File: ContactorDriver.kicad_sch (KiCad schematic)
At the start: 42 parts, among them J1 PowerConn, J10 FanConn3, J11 FanConn4, J2 DashboardConnA, J3 ContactorAConn, J4 DashboardConnB, J5 ContactorBConn, J6 DashboardConnC, J7 ContactorCConn, J8 FanConn1, J9 FanConn2, Q1 NDS356AP-VB, Q2 IRLML0030TRPbF, Q3 IRLML0030TRPbF, Q4 IRLML0030TRPbF

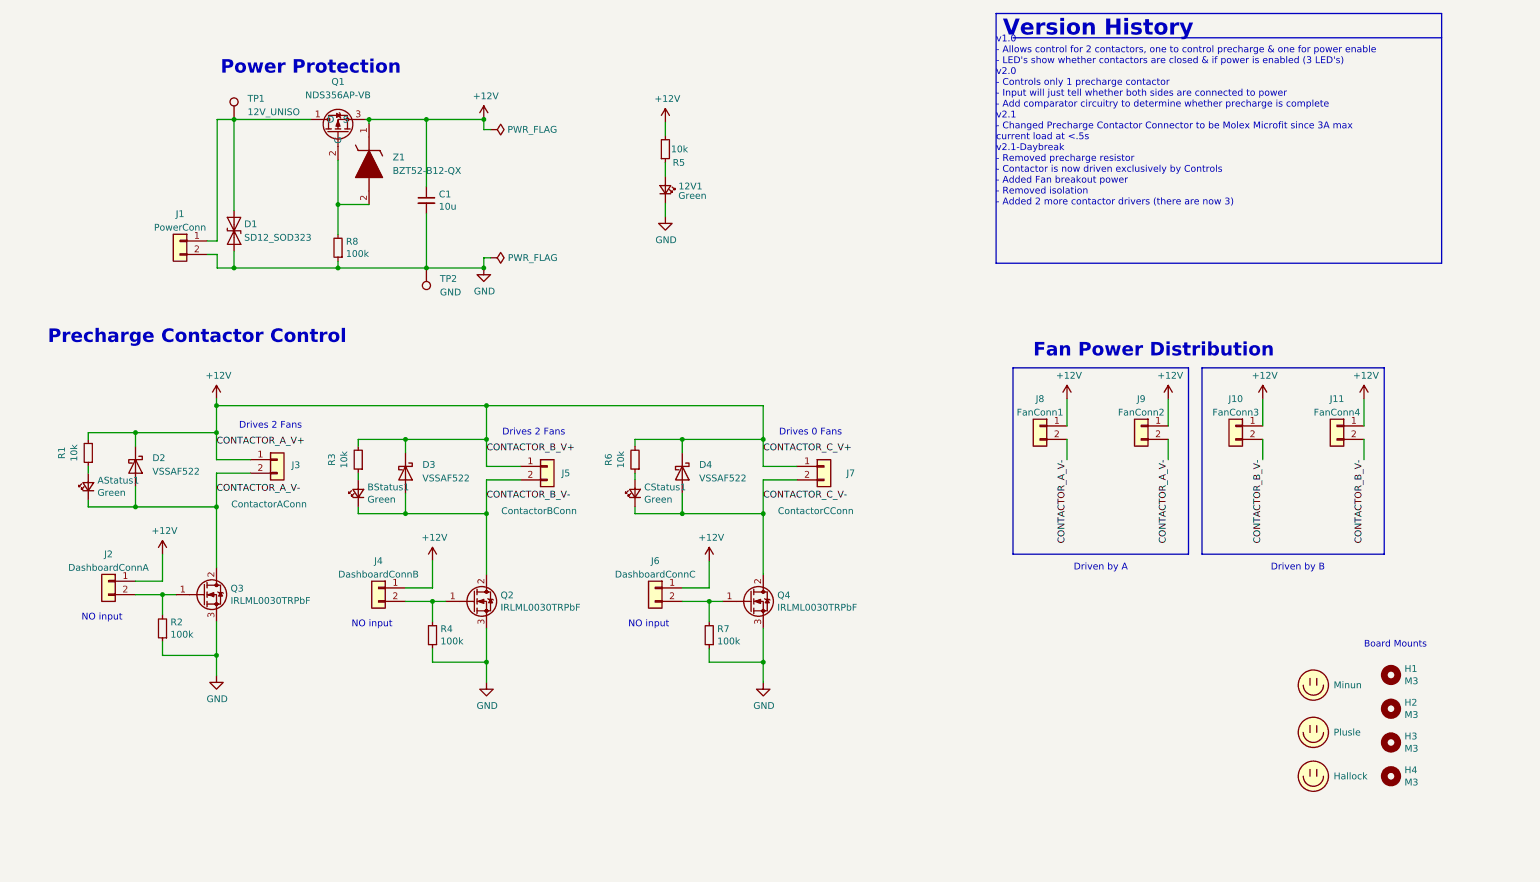
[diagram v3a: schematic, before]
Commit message: Updated BOM, PDFs, and added labels for tps
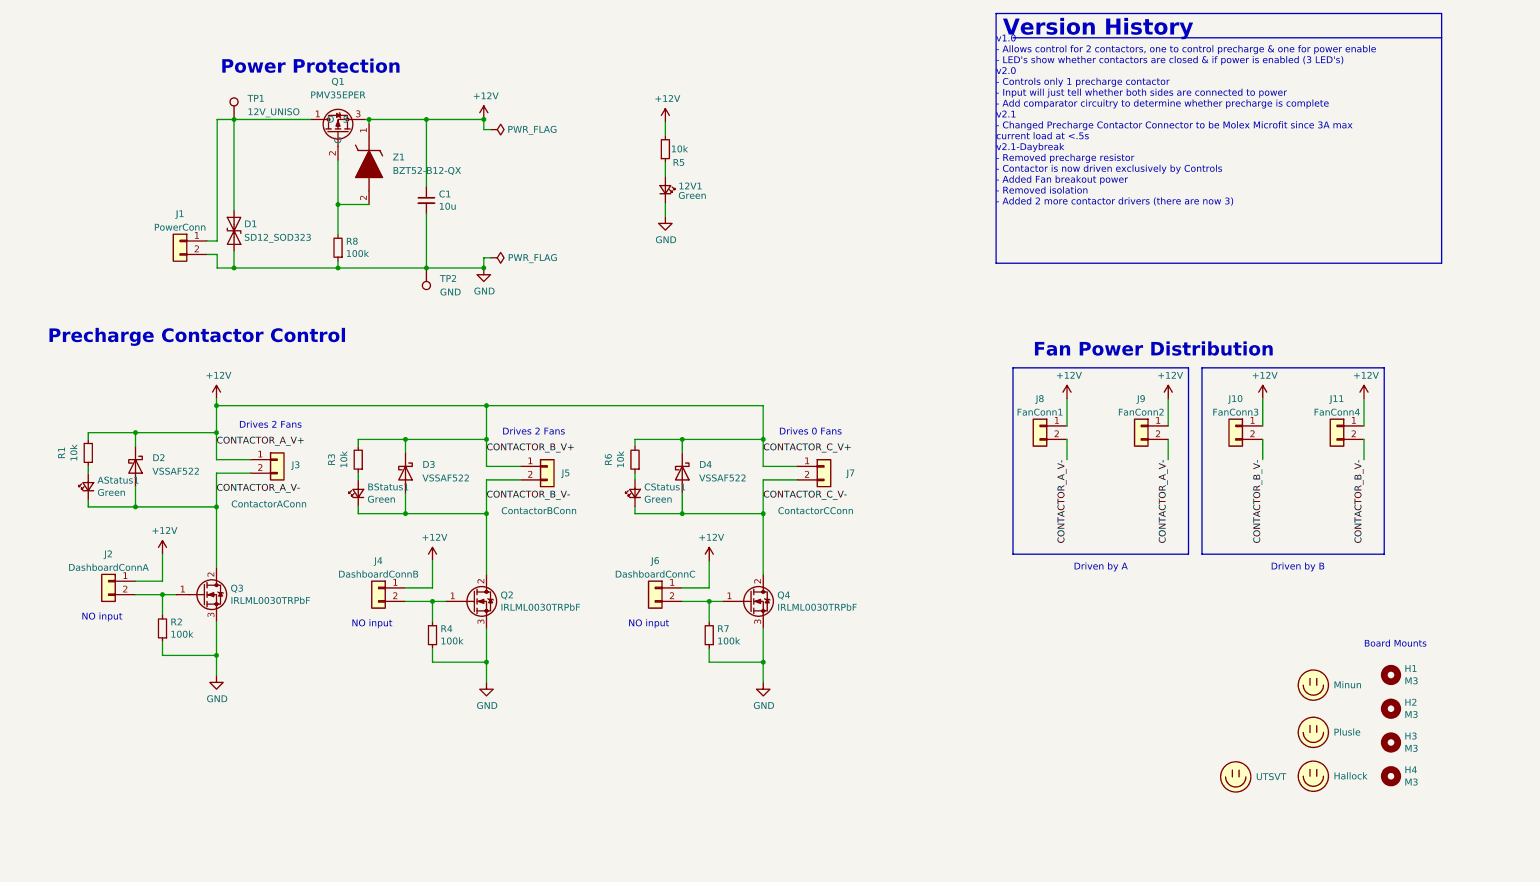
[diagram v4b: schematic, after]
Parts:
- added LOGO4: UTSVT, UTSVT_Special:UTSVT_Logo_Symbol, symbol utsvt-misc:Logo_Placeholder
- Q1: value NDS356AP-VB -> PMV35EPER; footprint Package_TO_SOT_SMD:SOT-23 -> Package_TO_SOT_SMD:SOT-23-3
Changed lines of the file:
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@@
 			)
 		)
-		(property "Value" "NDS356AP-VB"
+		(property "Value" "PMV35EPER"
 			(at 74.93 29.21 90)
 			(effects
@@
 			)
 		)
-		(property "Footprint" "Package_TO_SOT_SMD:SOT-23"
+		(property "Footprint" "Package_TO_SOT_SMD:SOT-23-3"
 			(at 61.722 34.798 0)
 			(effects
@@
 			)
 		)
-		(property "Datasheet" "https://www.lcsc.com/datasheet/lcsc_datasheet_2211010930_VBsemi-Elec-NDS356AP-VB_C710027.pdf"
+		(property "Datasheet" "https://www.mouser.com/datasheet/2/916/PMV35EPE-1539905.pdf"
 			(at 88.138 29.718 0)
 			(effects
@@
 			)
 		)
-		(property "Description" "30V 5.6A 46mΩ@10V,4.4A 2.5W 2V@250uA 1 Piece P-Channel SOT-23 MOSFETs ROHS"
+		(property "Description" "30V 5.3A 45mΩ@10V,4.4A 2.5W 2V@250uA 1 Piece P-Channel SOT-23 MOSFETs ROHS"
 			(at 90.932 27.686 0)
 			(effects
@@
 					(unit 1)
 				)
+			)
+		)
+	)
+	(symbol
+		(lib_id "utsvt-misc:Logo_Placeholder")
+		(at 243.84 157.48 0)
+		(unit 1)
+		(exclude_from_sim no)
+		(in_bom yes)
+		(on_board yes)
+		(dnp no)
+		(fields_autoplaced yes)
+		(property "Reference" "LOGO4"
+			(at 243.84 153.67 0)
+			(effects
+				(font
+					(size 1.27 1.27)
+				)
+				(hide yes)
+			)
+		)
+		(property "Value" "UTSVT"
+			(at 247.65 157.4799 0)
+			(effects
+				(font
+					(size 1.27 1.27)
+				)
+				(justify left)
+			)
+		)
+		(property "Footprint" "UTSVT_Special:UTSVT_Logo_Symbol"
+			(at 243.84 155.575 0)
+			(effects
+				(font
+					(size 1.27 1.27)
+				)
+				(hide yes)
+			)
+		)
+		(property "Datasheet" ""
+			(at 243.84 155.575 0)
+			(effects
+				(font
+					(size 1.27 1.27)
+				)
+				(hide yes)
+			)
+		)
+		(property "Description" "Graph footprint placeholder"
+			(at 243.84 157.48 0)
+			(effects
+				(font
+					(size 1.27 1.27)
+				)
+				(hide yes)
+			)
+		)
+		(instances
+			(project "ContactorDriver"
+				(path "/aaa5c8ef-bb12-4c4a-bd2b-ddbca3d09ae8"
+					(reference "LOGO4")
+					(unit 1)
+				)

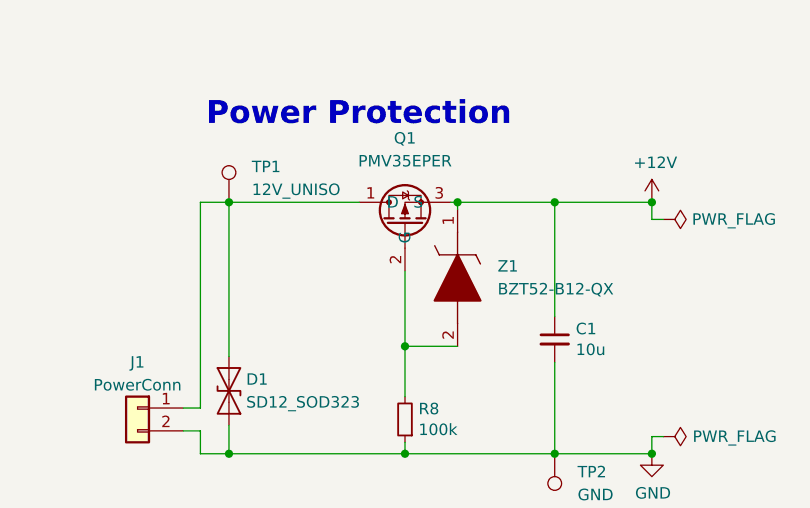
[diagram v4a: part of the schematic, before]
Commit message: fixed the pmos pinout
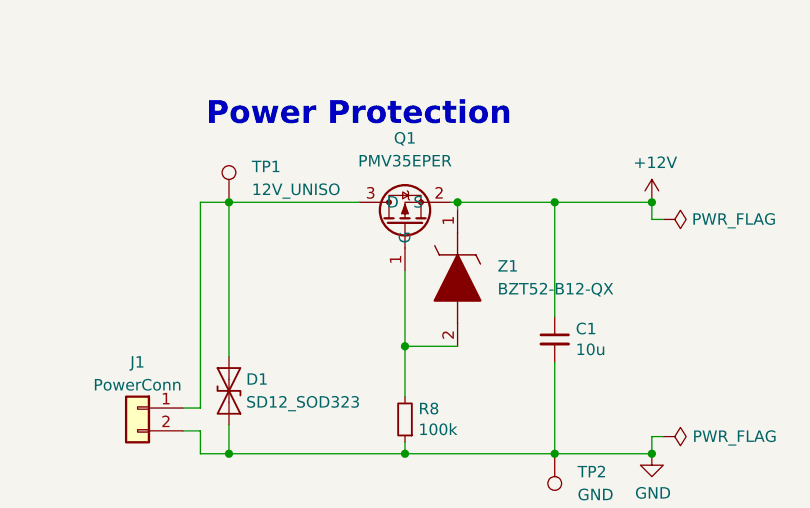
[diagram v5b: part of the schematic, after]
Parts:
- Q1: footprint Package_TO_SOT_SMD:SOT-23-3 -> Package_TO_SOT_SMD:SOT-23; symbol utsvt-chips:NDS356AP-VB -> utsvt-chips:PMV35EPE
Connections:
- net +12V: now also Q1.2 (S); no longer Q1.3 (S)
- net at D1.2 (A2), J1.1 (Pin_1), TP1.1: now also Q1.3 (D); no longer Q1.1 (D)
- net at R8.2, Z1.2: now also Q1.1 (G); no longer Q1.2 (G)
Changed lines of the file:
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@@
 	)
 	(symbol
-		(lib_id "utsvt-chips:NDS356AP-VB")
+		(lib_id "utsvt-chips:PMV35EPE")
 		(at 74.93 35.052 90)
 		(unit 1)
@@
 			)
 		)
-		(property "Footprint" "Package_TO_SOT_SMD:SOT-23-3"
+		(property "Footprint" "Package_TO_SOT_SMD:SOT-23"
 			(at 61.722 34.798 0)
 			(effects
@@
 			)
 		)
-		(property "Description" "30V 5.3A 45mΩ@10V,4.4A 2.5W 2V@250uA 1 Piece P-Channel SOT-23 MOSFETs ROHS"
+		(property "Description" "30 V, P-channel Trench MOSFET"
 			(at 90.932 27.686 0)
 			(effects

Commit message: added sense
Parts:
- removed J2: DashboardConnA, Connector_Molex:Molex_Micro-Fit_3.0_43650-0215_1x02_P3.00mm_Vertical, symbol Connector_Generic:Conn_01x02
- removed J3: ContactorAConn, Connector_Molex:Molex_Micro-Fit_3.0_43650-0215_1x02_P3.00mm_Vertical, symbol Connector_Generic:Conn_01x02
- removed J4: DashboardConnB, Connector_Molex:Molex_Micro-Fit_3.0_43650-0215_1x02_P3.00mm_Vertical, symbol Connector_Generic:Conn_01x02
- removed J5: ContactorBConn, Connector_Molex:Molex_Micro-Fit_3.0_43650-0215_1x02_P3.00mm_Vertical, symbol Connector_Generic:Conn_01x02
- removed J6: DashboardConnC, Connector_Molex:Molex_Micro-Fit_3.0_43650-0215_1x02_P3.00mm_Vertical, symbol Connector_Generic:Conn_01x02
- removed J7: ContactorCConn, Connector_Molex:Molex_Micro-Fit_3.0_43650-0215_1x02_P3.00mm_Vertical, symbol Connector_Generic:Conn_01x02
- added J12: ContactorAConn, UTSVT_Connectors:Molex_MicroFit3.0_1x4xP3.00mm_PolarizingPeg_Vertical, symbol Connector_Generic:Conn_01x04
- added J2: DashboardConnA, UTSVT_Connectors:Molex_MicroFit3.0_1x4xP3.00mm_PolarizingPeg_Vertical, symbol Connector_Generic:Conn_01x04
- added J3: ContactorBConn, UTSVT_Connectors:Molex_MicroFit3.0_1x4xP3.00mm_PolarizingPeg_Vertical, symbol Connector_Generic:Conn_01x04
- added J4: DashboardConnB, UTSVT_Connectors:Molex_MicroFit3.0_1x4xP3.00mm_PolarizingPeg_Vertical, symbol Connector_Generic:Conn_01x04
- added J5: ContactorCConn, UTSVT_Connectors:Molex_MicroFit3.0_1x4xP3.00mm_PolarizingPeg_Vertical, symbol Connector_Generic:Conn_01x04
- added J6: DashboardConnC, UTSVT_Connectors:Molex_MicroFit3.0_1x4xP3.00mm_PolarizingPeg_Vertical, symbol Connector_Generic:Conn_01x04
- added R10, R11, R9: 510, Resistor_SMD:R_0805_2012Metric_Pad1.20x1.40mm_HandSolder, symbol Device:R
- added U1, U2, U3: SFH617A-1, Package_DIP:DIP-4_W7.62mm, symbol Isolator:SFH617A-1
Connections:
- net +12V: now also J12.1 (Pin_1), J12.3 (Pin_3), J2.4 (Pin_4), J3.1 (Pin_1), J3.3 (Pin_3), J4.4 (Pin_4), J5.1 (Pin_1), J5.3 (Pin_3), J6.4 (Pin_4)
- net CONTACTOR_A_V-: now also J12.2 (Pin_2)
- net CONTACTOR_B_V-: now also J3.2 (Pin_2)
- net CONTACTOR_C_V-: now also J5.2 (Pin_2)
- net at Q3.1 (G), R2.2: now also J2.3 (Pin_3)
- net at Q4.1 (G), R7.2: now also J6.3 (Pin_3)
- net at Q2.1 (G), R4.2: now also J4.3 (Pin_3)
- new net: R10.2, U2.1
- new net: R9.2, U1.1
- new net: R11.2, U3.1
- new net AUX_A+: J2.2 (Pin_2), U1.4
- new net AUX_A-: J2.1 (Pin_1), U1.3
- new net AUX_B+: J4.2 (Pin_2), U2.4
- new net AUX_B-: J4.1 (Pin_1), U2.3
- new net AUX_C+: J6.2 (Pin_2), U3.4
- new net AUX_C-: J6.1 (Pin_1), U3.3
- new net GNDPWR: U1.2, U2.2, U3.2
- new net SENSE_A: J12.4 (Pin_4), R9.1
- new net SENSE_B: J3.4 (Pin_4), R10.1
- new net SENSE_C: J5.4 (Pin_4), R11.1
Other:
- note removed: "NO input"
- moved on the sheet: AStatus1, BStatus1, CStatus1, D2, D3, D4, J10, J11, J8, J9, Q2, Q3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

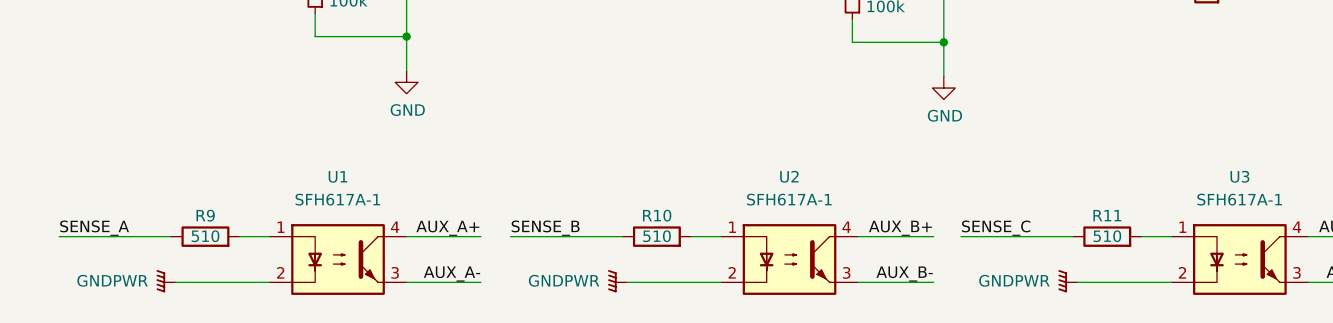
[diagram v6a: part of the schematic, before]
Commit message: layout changes for sense
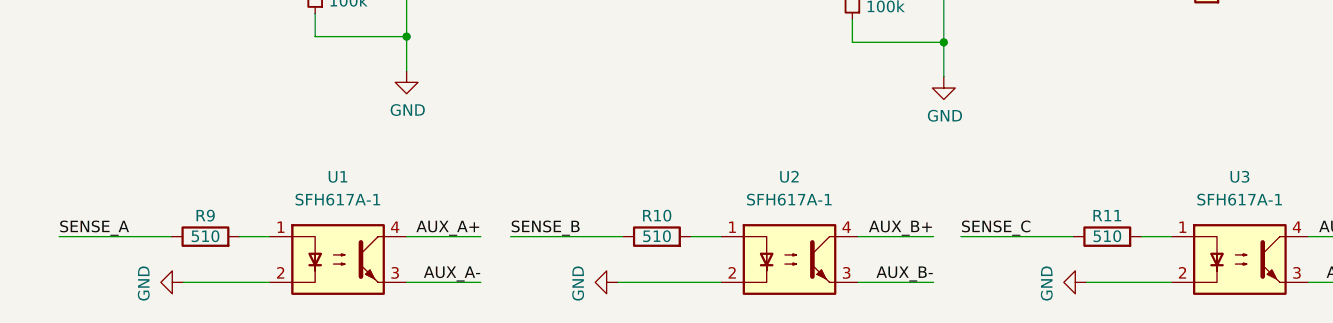
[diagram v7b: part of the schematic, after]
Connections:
- net GNDPWR is gone; now on net GND: U1.2, U2.2, U3.2
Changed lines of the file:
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@@
 	(wire
 		(pts
-			(xy 30.861 161.29) (xy 41.275 161.29)
+			(xy 132.08 161.29) (xy 141.478 161.29)
 		)
 		(stroke
@@
 	(wire
 		(pts
+			(xy 80.01 161.29) (xy 91.44 161.29)
+		)
+		(stroke
+			(width 0)
+			(type default)
+		)
+	)
+	(wire
+		(pts
 			(xy 55.372 33.782) (xy 55.372 50.927)
 		)
@@
 	(wire
 		(pts
-			(xy 131.064 161.29) (xy 141.478 161.29)
-		)
-		(stroke
-			(width 0)
-			(type default)
-		)
-	)
-	(wire
-		(pts
 			(xy 176.53 93.345) (xy 176.53 98.425)
 		)
@@
 	(wire
 		(pts
+			(xy 31.75 161.29) (xy 41.275 161.29)
+		)
+		(stroke
+			(width 0)
+			(type default)
+		)
+	)
+	(wire
+		(pts
 			(xy 55.372 58.547) (xy 55.372 61.722)
 		)
@@
 	(wire
 		(pts
-			(xy 81.026 161.29) (xy 91.44 161.29)
-		)
-		(stroke
-			(width 0)
-			(type default)
-		)
-	)
-	(wire
-		(pts
 			(xy 176.53 98.425) (xy 194.31 98.425)
 		)
@@
 	)
 	(symbol
+		(lib_id "power:GND")
+		(at 132.08 161.29 270)
+		(unit 1)
+		(exclude_from_sim no)
+		(in_bom yes)
+		(on_board yes)
+		(dnp no)
+		(property "Reference" "#PWR021"
+			(at 125.73 161.29 0)
+			(effects
+				(font
+					(size 1.27 1.27)
+				)
+				(hide yes)
+			)
+		)
+		(property "Value" "GND"
+			(at 127.6858 161.417 0)
+			(effects
+				(font
+					(size 1.27 1.27)
+				)
+			)
+		)
+		(property "Footprint" ""
+			(at 132.08 161.29 0)
+			(effects
+				(font
+					(size 1.27 1.27)
+				)
+				(hide yes)
+			)
+		)
+		(property "Datasheet" ""
+			(at 132.08 161.29 0)
+			(effects
+				(font
+					(size 1.27 1.27)
+				)
+				(hide yes)
+			)
+		)
+		(property "Description" ""
+			(at 132.08 161.29 0)
+			(effects
+				(font
+					(size 1.27 1.27)
+				)
+				(hide yes)
+			)
+		)
+		(pin "1"
+		)
+		(instances
+			(project "ContactorDriver"
+				(path "/aaa5c8ef-bb12-4c4a-bd2b-ddbca3d09ae8"
+					(reference "#PWR021")
+					(unit 1)
+				)
+			)
+		)
+	)
+	(symbol
 		(lib_id "Connector_Generic:Conn_01x02")
 		(at 234.315 81.915 0)
@@
 	)
 	(symbol
-		(lib_id "power:GNDPWR")
-		(at 81.026 161.29 270)
-		(unit 1)
-		(exclude_from_sim no)
-		(in_bom yes)
-		(on_board yes)
-		(dnp no)
-		(fields_autoplaced yes)
-		(property "Reference" "#PWR020"
-			(at 75.946 161.29 0)
-			(effects
-				(font
-					(size 1.27 1.27)
-				)
-				(hide yes)
-			)
-		)
-		(property "Value" "GNDPWR"
-			(at 77.978 161.1629 90)
-			(effects
-				(font
-					(size 1.27 1.27)
-				)
-				(justify right)
-			)
-		)
-		(property "Footprint" ""
-			(at 79.756 161.29 0)
-			(effects
-				(font
-					(size 1.27 1.27)
-				)
-				(hide yes)
-			)
-		)
-		(property "Datasheet" ""
-			(at 79.756 161.29 0)
-			(effects
-				(font
-					(size 1.27 1.27)
-				)
-				(hide yes)
-			)
-		)
-		(property "Description" "Power symbol creates a global label with name \"GNDPWR\" , global ground"
-			(at 81.026 161.29 0)
-			(effects
-				(font
-					(size 1.27 1.27)
-				)
-				(hide yes)
-			)
-		)
-		(pin "1"
-		)
-		(instances
-			(project "ContactorDriver"
-				(path "/aaa5c8ef-bb12-4c4a-bd2b-ddbca3d09ae8"
-					(reference "#PWR020")
-					(unit 1)
-				)
-			)
-		)
-	)
-	(symbol
 		(lib_id "Device:R_Small")
 		(at 106.045 129.54 180)
@@
 	)
 	(symbol
-		(lib_id "power:GNDPWR")
-		(at 131.064 161.29 270)
-		(unit 1)
-		(exclude_from_sim no)
-		(in_bom yes)
-		(on_board yes)
-		(dnp no)
-		(fields_autoplaced yes)
-		(property "Reference" "#PWR021"
-			(at 125.984 161.29 0)
-			(effects
-				(font
-					(size 1.27 1.27)
-				)
-				(hide yes)
-			)
-		)
-		(property "Value" "GNDPWR"
-			(at 128.016 161.1629 90)
-			(effects
-				(font
-					(size 1.27 1.27)
-				)
-				(justify right)
-			)
-		)
-		(property "Footprint" ""
-			(at 129.794 161.29 0)
-			(effects
-				(font
-					(size 1.27 1.27)
-				)
-				(hide yes)
-			)
-		)
-		(property "Datasheet" ""
-			(at 129.794 161.29 0)
-			(effects
-				(font
-					(size 1.27 1.27)
-				)
-				(hide yes)
-			)
-		)
-		(property "Description" "Power symbol creates a global label with name \"GNDPWR\" , global ground"
-			(at 131.064 161.29 0)
-			(effects
-				(font
-					(size 1.27 1.27)
-				)
-				(hide yes)
-			)
-		)
-		(pin "1"
-		)
-		(instances
-			(project "ContactorDriver"
-				(path "/aaa5c8ef-bb12-4c4a-bd2b-ddbca3d09ae8"
-					(reference "#PWR021")
-					(unit 1)
-				)
-			)
-		)
-	)
-	(symbol
 		(lib_id "Device:R_Small")
 		(at 152.4 97.155 180)
@@
 	)
 	(symbol
+		(lib_id "power:GND")
+		(at 80.01 161.29 270)
+		(unit 1)
+		(exclude_from_sim no)
+		(in_bom yes)
+		(on_board yes)
+		(dnp no)
+		(property "Reference" "#PWR020"
+			(at 73.66 161.29 0)
+			(effects
+				(font
+					(size 1.27 1.27)
+				)
+				(hide yes)
+			)
+		)
+		(property "Value" "GND"
+			(at 75.6158 161.417 0)
+			(effects
+				(font
+					(size 1.27 1.27)
+				)
+			)
+		)
+		(property "Footprint" ""
+			(at 80.01 161.29 0)
+			(effects
+				(font
+					(size 1.27 1.27)
+				)
+				(hide yes)
+			)
+		)
+		(property "Datasheet" ""
+			(at 80.01 161.29 0)
+			(effects
+				(font
+					(size 1.27 1.27)
+				)
+				(hide yes)
+			)
+		)
+		(property "Description" ""
+			(at 80.01 161.29 0)
+			(effects
+				(font
+					(size 1.27 1.27)
+				)
+				(hide yes)
+			)
+		)
+		(pin "1"
+		)
+		(instances
+			(project "ContactorDriver"
+				(path "/aaa5c8ef-bb12-4c4a-bd2b-ddbca3d09ae8"
+					(reference "#PWR020")
+					(unit 1)
+				)
+			)
+		)
+	)
+	(symbol
 		(lib_id "Device:R")
 		(at 84.328 156.21 90)
@@
 	)
 	(symbol
+		(lib_id "power:GND")
+		(at 31.75 161.29 270)
+		(unit 1)
+		(exclude_from_sim no)
+		(in_bom yes)
+		(on_board yes)
+		(dnp no)
+		(property "Reference" "#PWR019"
+			(at 25.4 161.29 0)
+			(effects
+				(font
+					(size 1.27 1.27)
+				)
+				(hide yes)
+			)
+		)
+		(property "Value" "GND"
+			(at 27.3558 161.417 0)
+			(effects
+				(font
+					(size 1.27 1.27)
+				)
+			)
+		)
+		(property "Footprint" ""
+			(at 31.75 161.29 0)
+			(effects
+				(font
+					(size 1.27 1.27)
+				)
+				(hide yes)
+			)
+		)
+		(property "Datasheet" ""
+			(at 31.75 161.29 0)
+			(effects
+				(font
+					(size 1.27 1.27)
+				)
+				(hide yes)
+			)
+		)
+		(property "Description" ""
+			(at 31.75 161.29 0)
+			(effects
+				(font
+					(size 1.27 1.27)
+				)
+				(hide yes)
+			)
+		)
+		(pin "1"
+		)
+		(instances
+			(project "ContactorDriver"
+				(path "/aaa5c8ef-bb12-4c4a-bd2b-ddbca3d09ae8"
+					(reference "#PWR019")
+					(unit 1)
+				)
+			)
+		)
+	)
+	(symbol
 		(lib_id "Connector_Generic:Conn_01x02")
 		(at 215.265 81.915 0)
@@
 					(unit 1)
 				)
-			)
-		)
-	)
-	(symbol
-		(lib_id "power:GNDPWR")
-		(at 30.861 161.29 270)
-		(unit 1)
-		(exclude_from_sim no)
-		(in_bom yes)
-		(on_board yes)
-		(dnp no)
-		(fields_autoplaced yes)
-		(property "Reference" "#PWR019"
-			(at 25.781 161.29 0)
-			(effects
-				(font
-					(size 1.27 1.27)
-				)
-				(hide yes)
-			)
-		)
-		(property "Value" "GNDPWR"
-			(at 27.813 161.1629 90)
-			(effects
-				(font
-					(size 1.27 1.27)
-				)
-				(justify right)
-			)
-		)
-		(property "Footprint" ""
-			(at 29.591 161.29 0)
-			(effects
-				(font
-					(size 1.27 1.27)
-				)
-				(hide yes)
-			)
-		)
-		(property "Datasheet" ""
-			(at 29.591 161.29 0)
-			(effects
-				(font
-					(size 1.27 1.27)
-				)
-				(hide yes)
-			)
-		)
-		(property "Description" "Power symbol creates a global label with name \"GNDPWR\" , global ground"
-			(at 30.861 161.29 0)
-			(effects
-				(font
-					(size 1.27 1.27)
-				)
-				(hide yes)
-			)
-		)
-		(pin "1"
-		)
-		(instances
-			(project "ContactorDriver"
-				(path "/aaa5c8ef-bb12-4c4a-bd2b-ddbca3d09ae8"
-					(reference "#PWR019")
-					(unit 1)
-				)
